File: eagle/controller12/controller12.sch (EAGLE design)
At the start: 61 parts, among them IC1 ILD213T, J2 AVR_SPI_PRG_6PTH, J5 FEMALE 2x3, Q1 FDD4141TO252, Q2 200mA/50V, Q3 FDD4141TO252, Q4 200mA/50V, Q5 200mA/50V, U3 MP2307, X1 1501_04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

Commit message: controller12: sidebar
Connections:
- net GND: no longer J5.6
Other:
- moved on the sheet: J5
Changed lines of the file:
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@@
 <part name="SUPPLY8" library="SparkFun-Aesthetics" deviceset="VCC" device=""/>
 <part name="J5" library="SparkFun-Connectors" deviceset="M03X2" device="FEMALE" value="FEMALE 2x3"/>
-<part name="GND21" library="SparkFun-Aesthetics" deviceset="GND" device=""/>
 <part name="D1" library="diode" library_urn="urn:adsk.eagle:library:210" deviceset="MBRS130LT3" device="" package3d_urn="urn:adsk.eagle:package:43404/2"/>
 <part name="GND23" library="supply1" library_urn="urn:adsk.eagle:library:371" deviceset="GNDA" device=""/>
@@
 <instance part="S2" gate="1" x="162.56" y="106.68"/>
 <instance part="SUPPLY8" gate="G$1" x="147.32" y="106.68" rot="R90"/>
-<instance part="J5" gate="G$1" x="81.28" y="93.98" rot="R180"/>
-<instance part="GND21" gate="1" x="71.12" y="101.6" rot="R180"/>
+<instance part="J5" gate="G$1" x="106.68" y="81.28" rot="R180"/>
 </instances>
 <busses>
@@
 <pinref part="GND29" gate="1" pin="GND"/>
 </segment>
-<segment>
-<pinref part="J5" gate="G$1" pin="6"/>
-<pinref part="GND21" gate="1" pin="GND"/>
-<wire x1="73.66" y1="96.52" x2="71.12" y2="96.52" width="0.1524" layer="91"/>
-<wire x1="71.12" y1="96.52" x2="71.12" y2="99.06" width="0.1524" layer="91"/>
-</segment>
 </net>
 <net name="RX" class="0">
@@
 <segment>
 <pinref part="J5" gate="G$1" pin="4"/>
-<wire x1="73.66" y1="93.98" x2="66.04" y2="93.98" width="0.1524" layer="91"/>
-<label x="66.04" y="93.98" size="1.778" layer="95" rot="R90"/>
+<wire x1="99.06" y1="81.28" x2="91.44" y2="81.28" width="0.1524" layer="91"/>
+<label x="91.44" y="81.28" size="1.778" layer="95" rot="R90"/>
 </segment>
 </net>
@@
 </segment>
 <segment>
-<wire x1="88.9" y1="96.52" x2="99.06" y2="96.52" width="0.1524" layer="91"/>
-<label x="99.06" y="96.52" size="1.778" layer="95" rot="R90"/>
+<wire x1="114.3" y1="83.82" x2="124.46" y2="83.82" width="0.1524" layer="91"/>
+<label x="124.46" y="83.82" size="1.778" layer="95" rot="R90"/>
 <pinref part="J5" gate="G$1" pin="5"/>
 </segment>
@@
 </segment>
 <segment>
-<wire x1="88.9" y1="93.98" x2="104.14" y2="93.98" width="0.1524" layer="91"/>
-<label x="104.14" y="93.98" size="1.778" layer="95" rot="R90"/>
+<wire x1="114.3" y1="81.28" x2="129.54" y2="81.28" width="0.1524" layer="91"/>
+<label x="129.54" y="81.28" size="1.778" layer="95" rot="R90"/>
 <pinref part="J5" gate="G$1" pin="3"/>
 </segment>
@@
 <segment>
 <pinref part="J5" gate="G$1" pin="1"/>
-<wire x1="88.9" y1="91.44" x2="106.68" y2="91.44" width="0.1524" layer="91"/>
-<label x="106.68" y="91.44" size="1.778" layer="95"/>
+<wire x1="114.3" y1="78.74" x2="132.08" y2="78.74" width="0.1524" layer="91"/>
+<label x="132.08" y="78.74" size="1.778" layer="95"/>
 </segment>
 <segment>
@@
 <segment>
 <pinref part="J5" gate="G$1" pin="2"/>
-<wire x1="73.66" y1="91.44" x2="60.96" y2="91.44" width="0.1524" layer="91"/>
-<label x="60.96" y="91.44" size="1.778" layer="95" rot="R90"/>
-</segment>
-<segment>
+<wire x1="99.06" y1="78.74" x2="86.36" y2="78.74" width="0.1524" layer="91"/>
+<label x="86.36" y="78.74" size="1.778" layer="95" rot="R90"/>
+</segment>
+<segment>

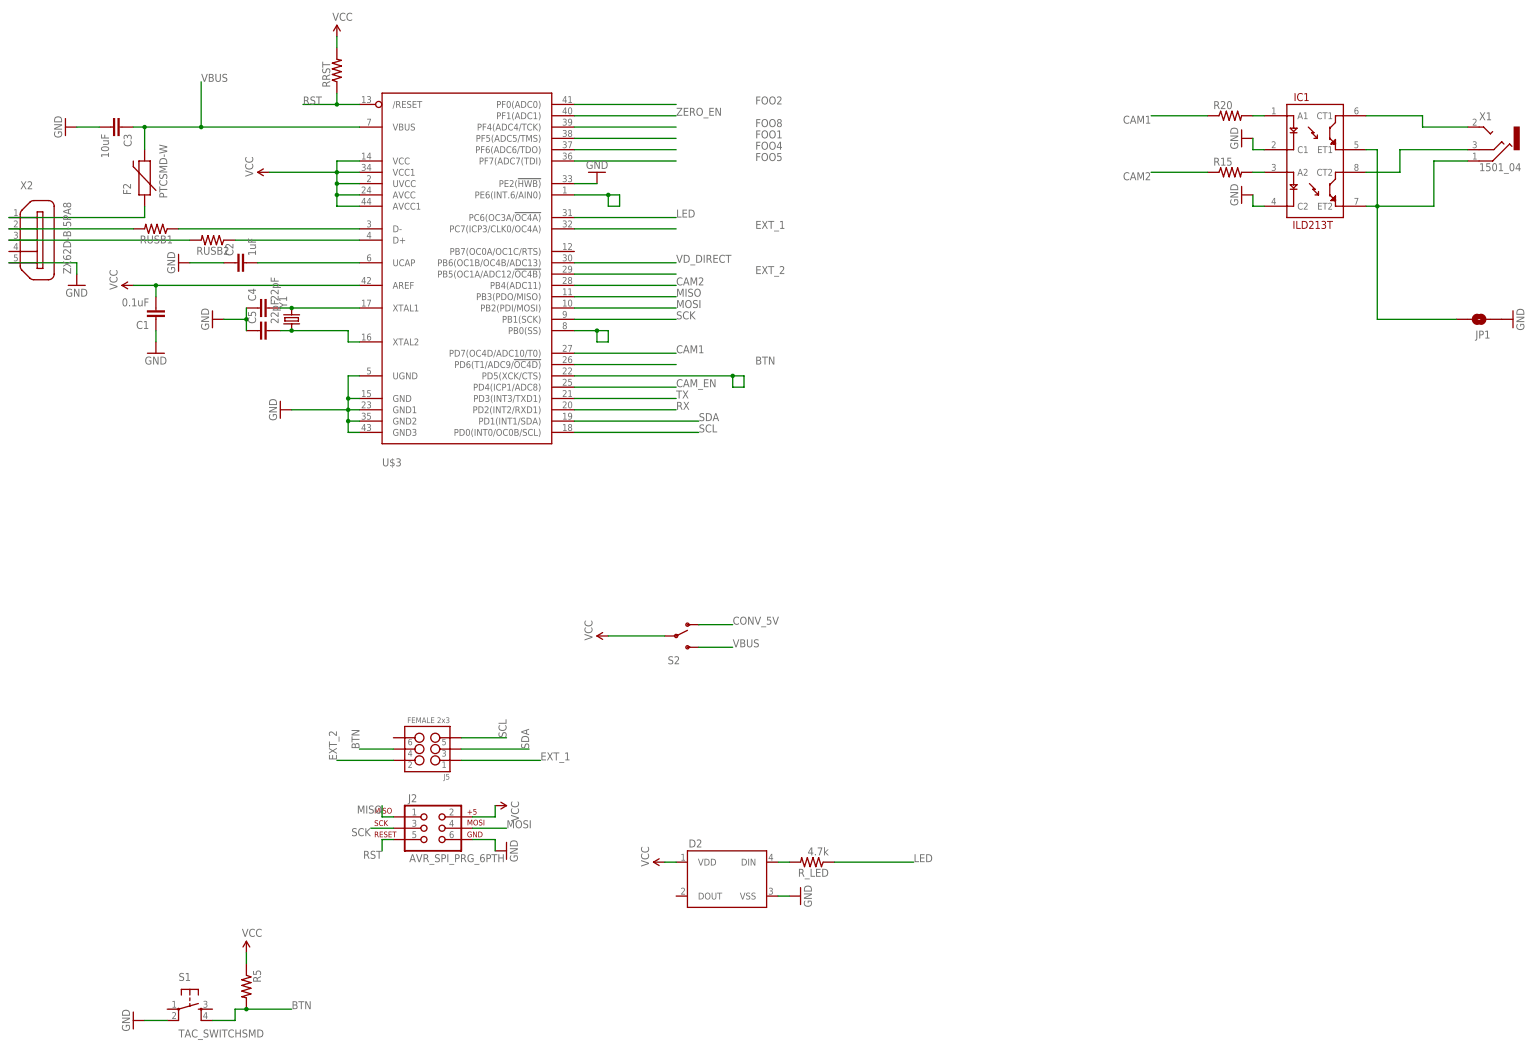
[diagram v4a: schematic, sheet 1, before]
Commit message: controller12: added 5k resistor to allow to use AREF either with a voltage divider, without one or not at all
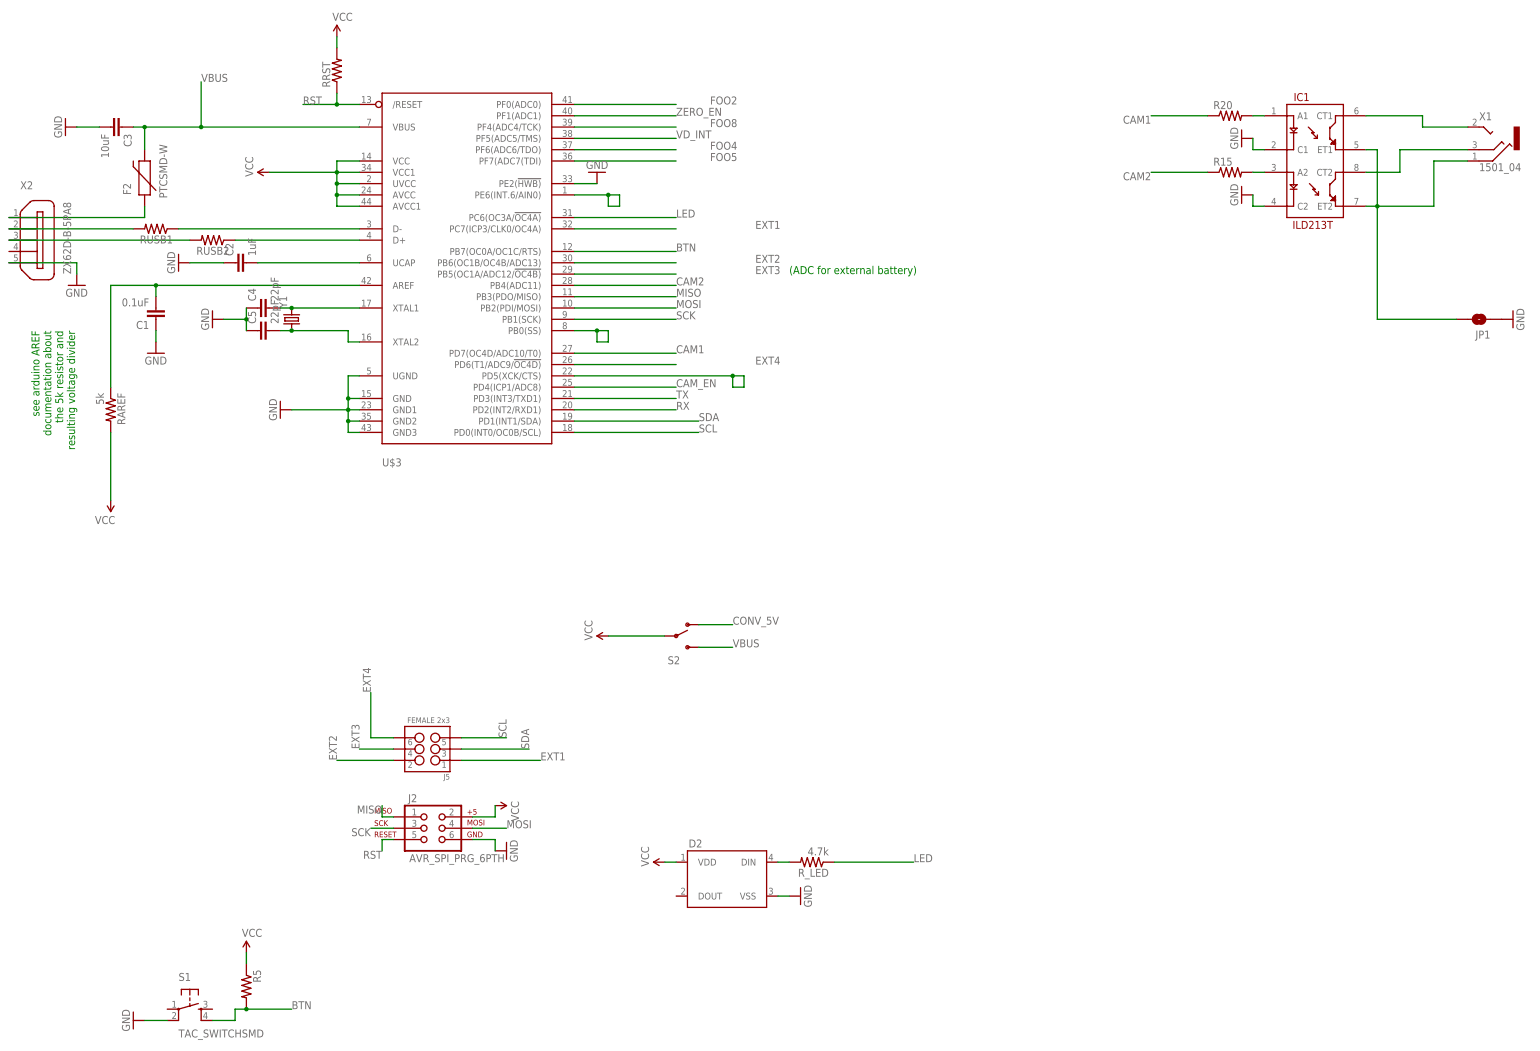
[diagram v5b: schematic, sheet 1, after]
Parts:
- removed D1: MBRS130LT3, diode:MBRS130LT3
- added RAREF: 5k, SparkFun-Passives:RESISTOR1206
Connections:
- net EXT_1 renamed EXT1
- removed net EXT_2: J5.2, U$3.PB5(OC1A/ADC12/!OC4B)
- removed net FOO1: U$3.PF5(ADC5/TMS)
- removed net VD_DIRECT: C6.1, U$3.PB6(OC1B/OC4B/ADC13), VD1.1, VD2.2
- new net EXT2: J5.2, U$3.PB6(OC1B/OC4B/ADC13)
- new net EXT3: J5.4, U$3.PB5(OC1A/ADC12/!OC4B)
- new net EXT4: J5.6, U$3.PD6(T1/ADC9/!OC4D)
- new net N$18: C1.2, RAREF.1, U$3.AREF
- new net VD_INT: C6.1, U$3.PF5(ADC5/TMS), VD1.1, VD2.2
- net BTN: now also U$3.PB7(OC0A/OC1C/RTS); no longer J5.4, U$3.PD6(T1/ADC9/!OC4D)
- net GNDA: no longer D1.A
- net N$26: no longer D1.C
- net VCC: now also RAREF.2; no longer C1.2, U$3.AREF
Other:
- note added: "(ADC for external battery)"
- note added: "see arduino AREF documentation about the 5k resistor and resulting voltage divider"
